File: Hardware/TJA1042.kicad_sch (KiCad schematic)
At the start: 8 parts, among them J19 WAFER-GH1.25-2PWB, U45 TJA1042TK/3

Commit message: 拉线
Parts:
- renumbered C141 to C137, C142 to C138, C143 to C139, C144 to C140, J19 to J18, L9 to L8, R127 to R126, U45 to U44

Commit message: 修存档拉线
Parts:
- renumbered C137 to C110, C138 to C111, C139 to C112, C140 to C113, J18 to J20, U44 to U52

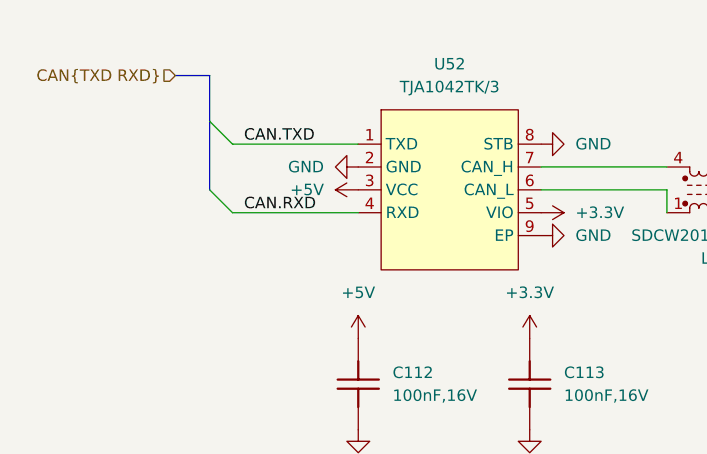
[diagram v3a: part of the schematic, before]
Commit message: PCB和foc_demo
PCB：
部分信号增加测试点
半桥增加栅极电容和RC吸收（待定），泄放mos是否需要栅极电容待测
软件：
增加foc_demo半成品
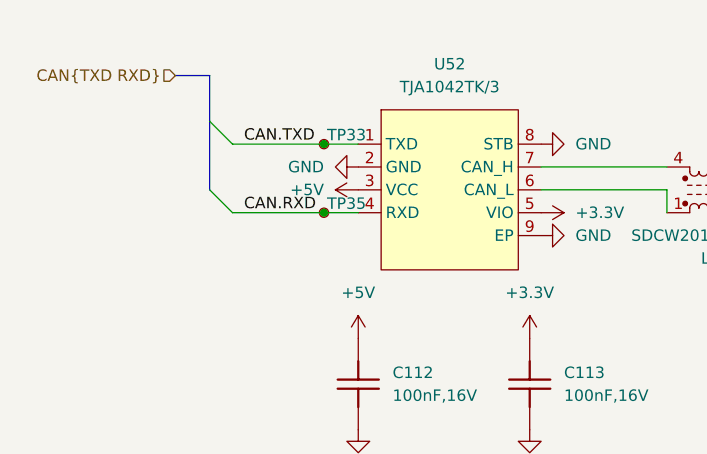
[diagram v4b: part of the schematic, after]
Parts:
- added TP33, TP35: ~, Library:test_point_0.5mm, symbol HPM6280Foc:test_point
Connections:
- net CAN.RXD: now also TP35.1
- net CAN.TXD: now also TP33.1
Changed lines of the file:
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@@
+		(color 0 0 0 0)
+	)
+	(junction
+		(at 91.44 96.52)
+		(diameter 0)
+		(color 0 0 0 0)
+	)
+	(junction
+		(at 91.44 104.14)
+		(diameter 0)
 		(color 0 0 0 0)
 	)
@@
 	(wire
 		(pts
+			(xy 91.44 96.52) (xy 95.25 96.52)
+		)
+		(stroke
+			(width 0)
+			(type default)
+		)
+	)
+	(wire
+		(pts
 			(xy 180.34 99.06) (xy 180.34 100.33)
 		)
@@
 	(wire
 		(pts
-			(xy 81.28 104.14) (xy 95.25 104.14)
-		)
-		(stroke
-			(width 0)
-			(type default)
-		)
-	)
-	(wire
-		(pts
-			(xy 81.28 96.52) (xy 95.25 96.52)
+			(xy 81.28 104.14) (xy 91.44 104.14)
+		)
+		(stroke
+			(width 0)
+			(type default)
+		)
+	)
+	(wire
+		(pts
+			(xy 81.28 96.52) (xy 91.44 96.52)
 		)
 		(stroke
@@
 		(pts
 			(xy 144.78 104.14) (xy 144.78 106.68)
+		)
+		(stroke
+			(width 0)
+			(type default)
+		)
+	)
+	(wire
+		(pts
+			(xy 91.44 104.14) (xy 95.25 104.14)
 		)
 		(stroke
@@
 			)
 			(justify right)
+		)
+	)
+	(symbol
+		(lib_id "HPM6280Foc:test_point")
+		(at 91.44 104.14 0)
+		(unit 1)
+		(exclude_from_sim no)
+		(in_bom yes)
+		(on_board yes)
+		(dnp no)
+		(property "Reference" "TP35"
+			(at 93.9502 103.124 0)
+			(effects
+				(font
+					(size 1.27 1.27)
+				)
+			)
+		)
+		(property "Value" "~"
+			(at 91.44 104.14 0)
+			(effects
+				(font
+					(size 1.27 1.27)
+				)
+				(hide yes)
+			)
+		)
+		(property "Footprint" "Library:test_point_0.5mm"
+			(at 91.44 104.14 0)
+			(effects
+				(font
+					(size 1.27 1.27)
+				)
+				(hide yes)
+			)
+		)
+		(property "Datasheet" ""
+			(at 91.44 104.14 0)
+			(effects
+				(font
+					(size 1.27 1.27)
+				)
+				(hide yes)
+			)
+		)
+		(property "Description" ""
+			(at 91.44 104.14 0)
+			(effects
+				(font
+					(size 1.27 1.27)
+				)
+				(hide yes)
+			)
+		)
+		(pin "1"
+		)
+		(instances
+			(project "HPM5E31_ECatDualFOC"
+				(path "/a07e9810-3899-4327-ba8f-f24142a7c70e/53f5766c-ec8f-4b40-a51f-916b133ba359"
+					(reference "TP36")
+					(unit 1)
+				)
+				(path "/a07e9810-3899-4327-ba8f-f24142a7c70e/c78eab24-5a2b-43f8-b2ca-bd8788f7483b"
+					(reference "TP35")
+					(unit 1)
+				)
+			)
 		)
 	)
@@
 					(unit 1)
 				)
+			)
+		)
+	)
+	(symbol
+		(lib_id "HPM6280Foc:test_point")
+		(at 91.44 96.52 0)
+		(unit 1)
+		(exclude_from_sim no)
+		(in_bom yes)
+		(on_board yes)
+		(dnp no)
+		(property "Reference" "TP33"
+			(at 93.9502 95.504 0)
+			(effects
+				(font
+					(size 1.27 1.27)
+				)
+			)
+		)
+		(property "Value" "~"
+			(at 91.44 96.52 0)
+			(effects
+				(font
+					(size 1.27 1.27)
+				)
+				(hide yes)
+			)
+		)
+		(property "Footprint" "Library:test_point_0.5mm"
+			(at 91.44 96.52 0)
+			(effects
+				(font
+					(size 1.27 1.27)
+				)
+				(hide yes)
+			)
+		)
+		(property "Datasheet" ""
+			(at 91.44 96.52 0)
+			(effects
+				(font
+					(size 1.27 1.27)
+				)
+				(hide yes)
+			)
+		)
+		(property "Description" ""
+			(at 91.44 96.52 0)
+			(effects
+				(font
+					(size 1.27 1.27)
+				)
+				(hide yes)
+			)
+		)
+		(pin "1"
+		)
+		(instances
+			(project "HPM5E31_ECatDualFOC"
+				(path "/a07e9810-3899-4327-ba8f-f24142a7c70e/53f5766c-ec8f-4b40-a51f-916b133ba359"
+					(reference "TP34")
+					(unit 1)
+				)
+				(path "/a07e9810-3899-4327-ba8f-f24142a7c70e/c78eab24-5a2b-43f8-b2ca-bd8788f7483b"
+					(reference "TP33")
+					(unit 1)
+				)
